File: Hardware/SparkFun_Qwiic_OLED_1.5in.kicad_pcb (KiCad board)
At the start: 2 copper layers, 34.3 x 48.3 mm, 59 parts, among them J1 Qwiic_RA, J2 Qwiic_RA, J3 Conn_01x06, U1 OLED_1.5in, U5 AP3012

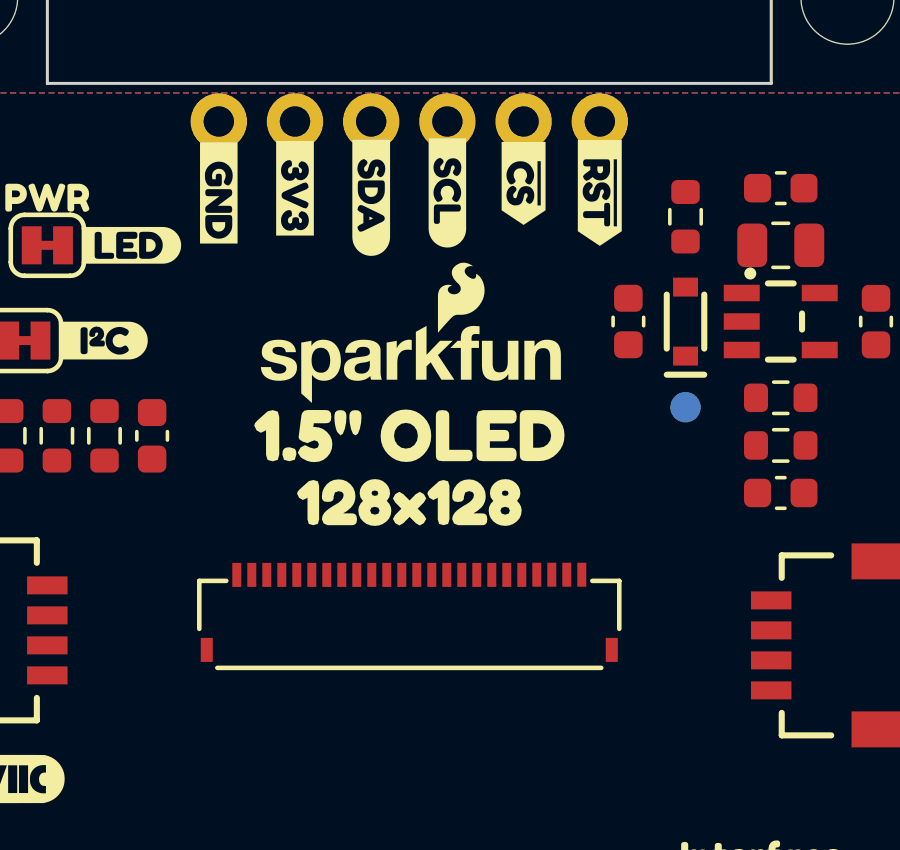
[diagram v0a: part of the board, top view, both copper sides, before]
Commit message: Removes connector from OLED symbol
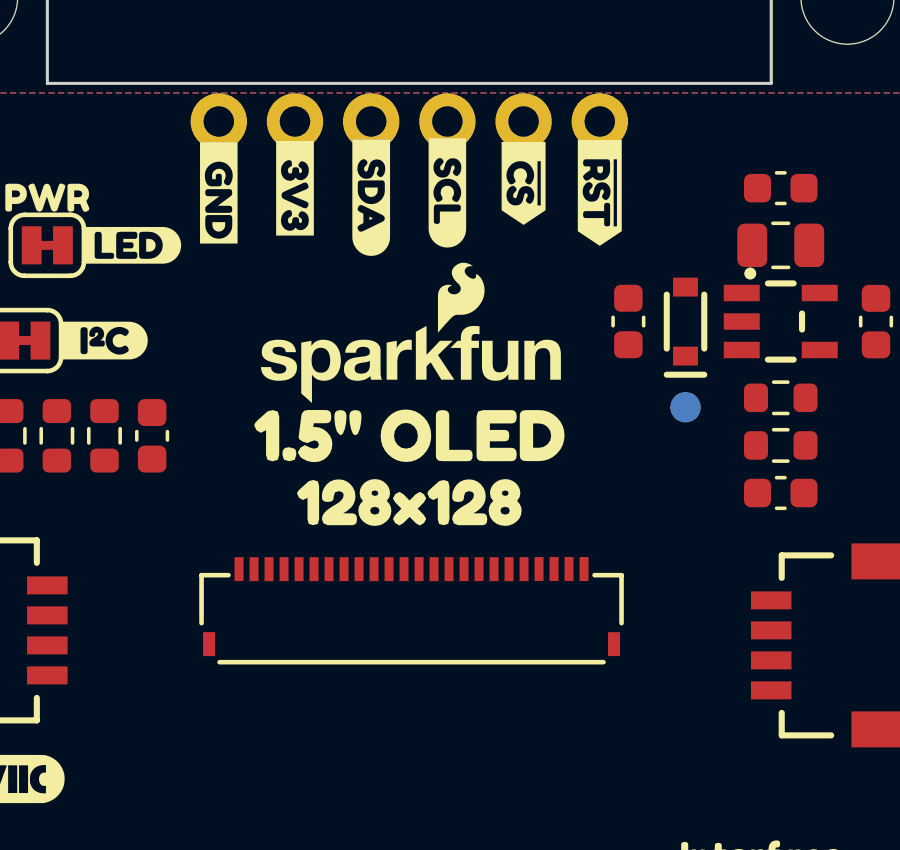
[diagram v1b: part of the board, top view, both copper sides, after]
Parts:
- removed R8: 10k, SparkFun-Resistor:R_0603_1608Metric
- removed U1: OLED_1.5in, SparkFun-Display:OLED_1.5in_128x128-Folded
- added J4: Conn_01x24_FPC, SparkFun-Connector:FPC_0.5mm-24, F.Cu at (140.5, 85.5)
- added U2: WEO128128ASAP3N00000, SparkFun-Display:OLED_1.5in_128x128-Folded, F.Cu at (140.4, 87.0)
- R6: value 634k -> 569k

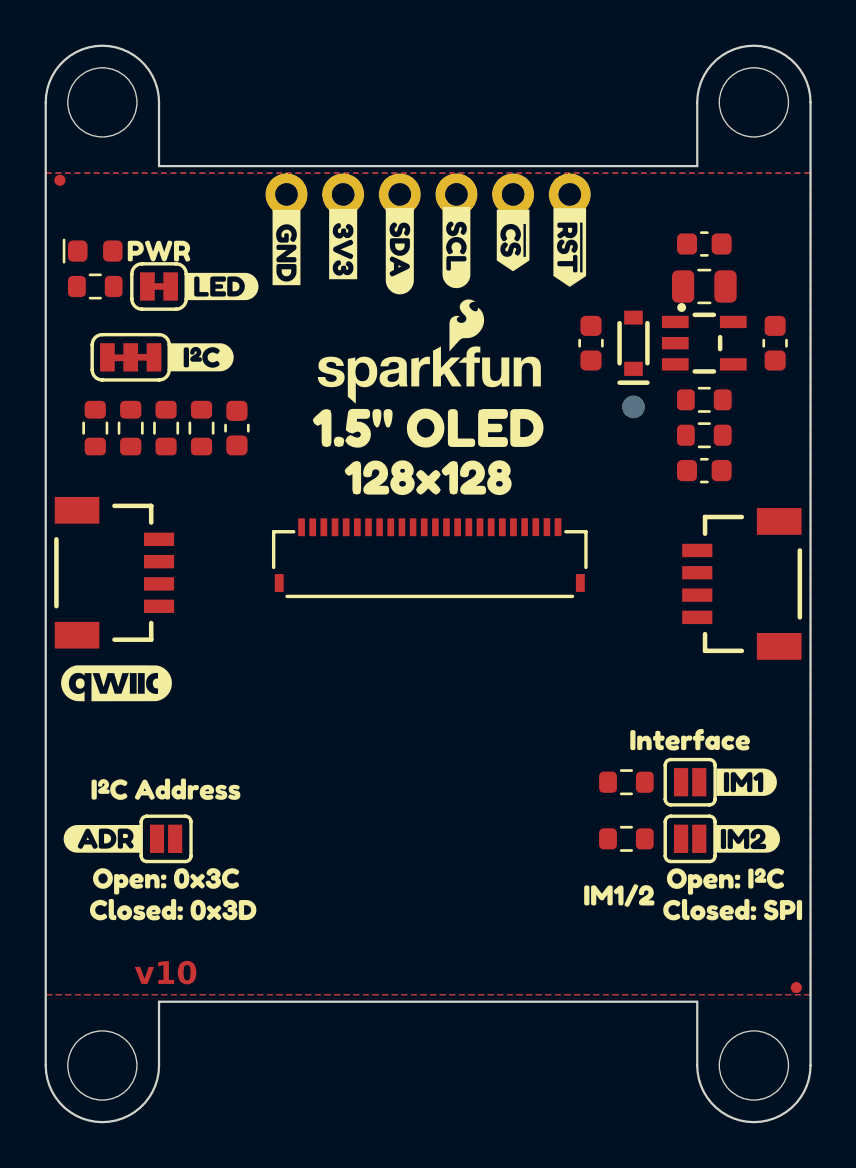
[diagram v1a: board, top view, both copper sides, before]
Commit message: Removes connector from OLED symbolbol and footprint
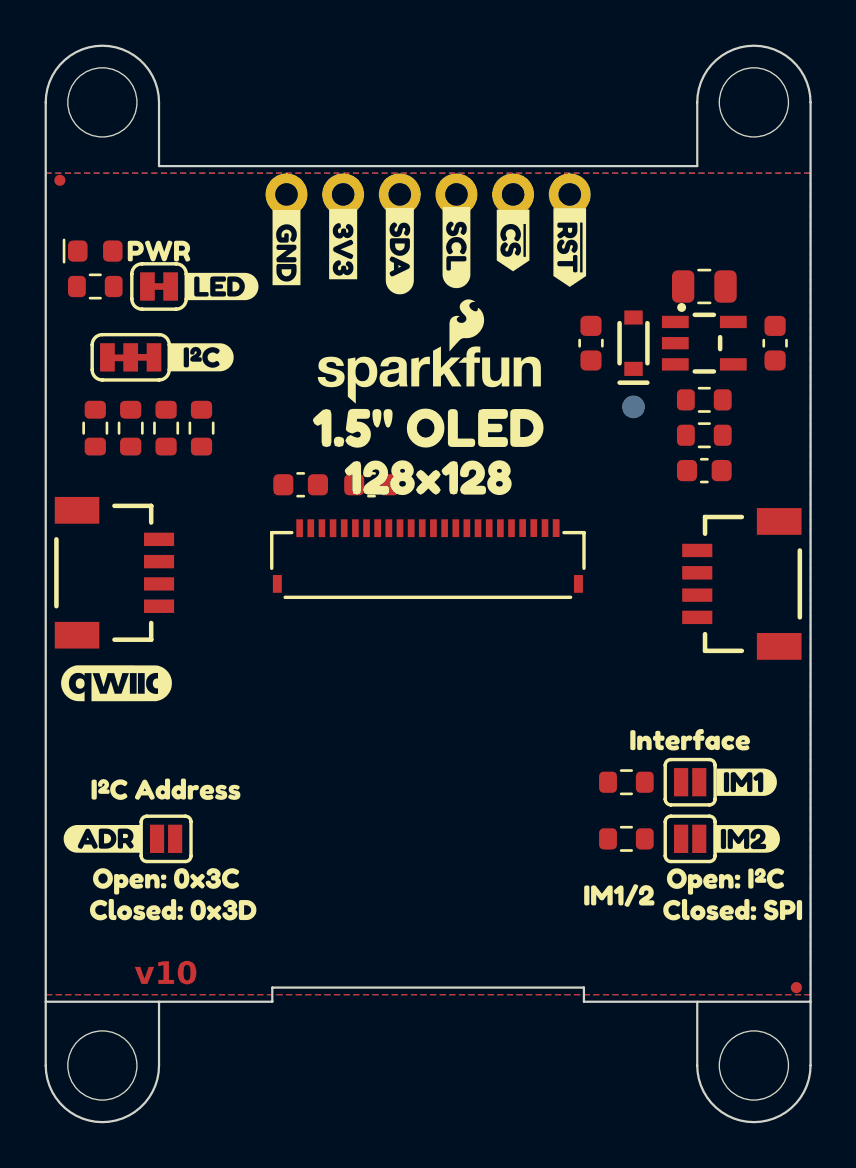
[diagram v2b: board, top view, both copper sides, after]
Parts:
- moved C4 18.4 mm to (137.9, 82.2), turned to 0 degrees
- moved C5 3.82 mm to (134.7, 82.2), turned to 180 degrees
- moved J4 0.10 mm to (140.4, 85.5)
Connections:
- J4 pad 13: unconnected-(J4-Pin_13-Pad13) -> GND
- J4 pad 14: unconnected-(J4-Pin_14-Pad14) -> GND
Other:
- outline, holes or cut-outs redrawn

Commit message: Aligns the power circuitry to the IC's specification
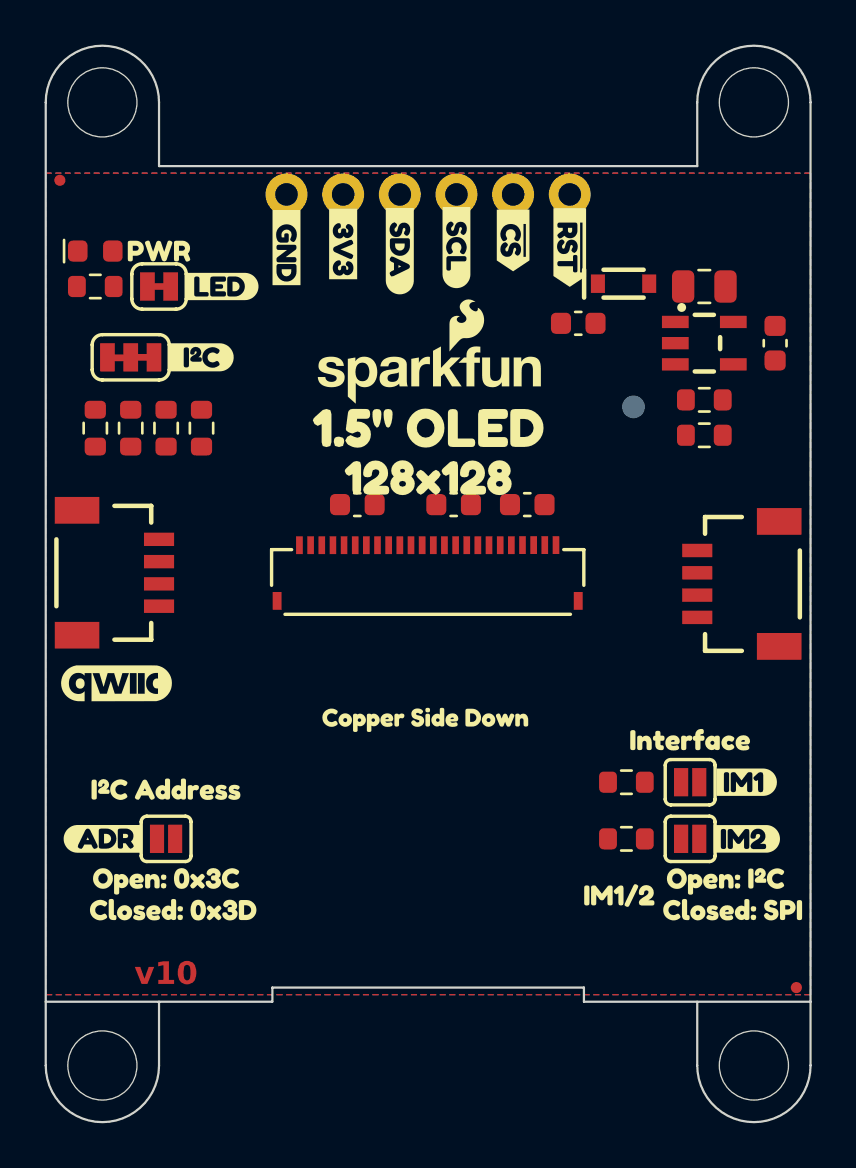
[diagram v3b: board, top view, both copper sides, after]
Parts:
- added kibuzzard-684C4DD6: G***, kibuzzard-684C4DD6, F.Cu at (140.3, 92.8)
- moved C3 15.6 mm to (137.2, 83.1)
- moved C5 10.2 mm to (144.9, 83.1)
- moved C4 3.79 mm to (141.6, 83.1), turned to 180 degrees
- moved D2 2.71 mm to (149.2, 73.2), turned to 0 degrees
- moved C2 1.06 mm to (147.1, 75.0), turned to 180 degrees
- moved J4 0.76 mm to (140.4, 86.3)
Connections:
- C3 pad 1: Net-(J4-Pin_3) -> Net-(J4-Pin_22)
- J4 pad 10: ~{CS} -> SCL/SCK
- J4 pad 11: ~{RST} -> GND
- J4 pad 12: Net-(J4-Pin_12) -> GND
- J4 pad 13: GND -> Net-(J4-Pin_13)
- J4 pad 14: GND -> ~{RST}
- J4 pad 15: SCL/SCK -> ~{CS}
- J4 pad 16: SDA/SDI -> Net-(J4-Pin_16)
- J4 pad 18: GND -> Net-(J4-Pin_18)
- J4 pad 19: GND -> Net-(J4-Pin_19)
- J4 pad 20: GND -> 3.3V
- J4 pad 21: GND -> 3.3V
- J4 pad 22: GND -> Net-(J4-Pin_22)
- J4 pad 3: Net-(J4-Pin_3) -> GND
- J4 pad 4: 3.3V -> GND
- J4 pad 5: 3.3V -> GND
- J4 pad 6: Net-(J4-Pin_6) -> GND
- J4 pad 7: Net-(J4-Pin_7) -> GND
- J4 pad 9: Net-(J4-Pin_9) -> SDA/SDI
- JP3 pad 1: Net-(J4-Pin_12) -> Net-(J4-Pin_13)
- JP6 pad 2: Net-(J4-Pin_6) -> Net-(J4-Pin_19)
- JP7 pad 1: Net-(J4-Pin_7) -> Net-(J4-Pin_18)
- R10 pad 2: Net-(J4-Pin_6) -> Net-(J4-Pin_19)
- R11 pad 1: Net-(J4-Pin_7) -> Net-(J4-Pin_18)
- R6 pad 2: Net-(J4-Pin_9) -> Net-(J4-Pin_16)
- R7 pad 2: Net-(J4-Pin_12) -> Net-(J4-Pin_13)

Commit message: Routes the power circuitry
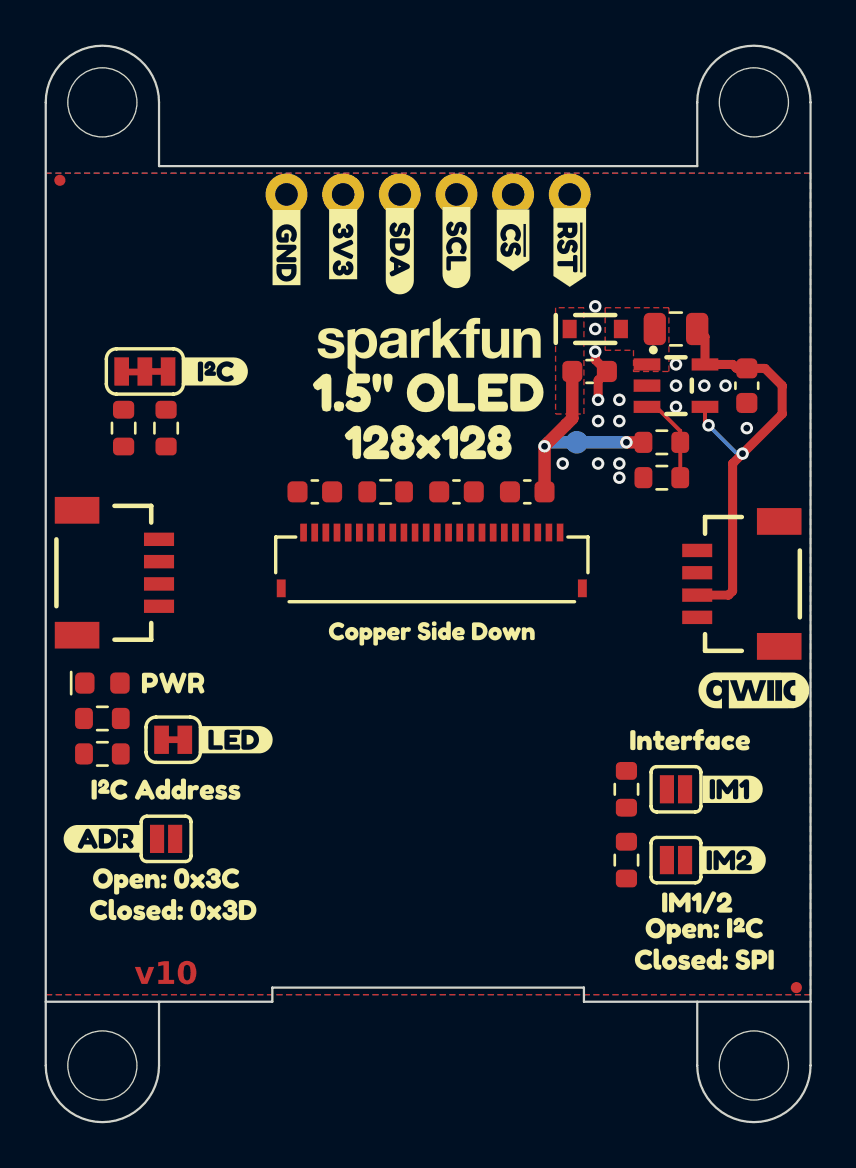
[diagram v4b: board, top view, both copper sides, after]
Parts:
- removed the G*** at (140.4, 77.2)
- added G***: LOGO, SparkFun-Aesthetic:SparkFun_Logo_NoFlame_10mm, F.Cu at (140.4, 75.9)
- moved G*** 28.6 mm to (155.0, 91.4)
- moved JP1 20.3 mm to (129.0, 93.7)
- moved kibuzzard-680FC883 20.3 mm to (131.8, 93.7)
- moved kibuzzard-65A8A8B4 19.4 mm to (129.0, 91.1)
- moved R3 19.4 mm to (125.8, 92.7)
- moved D1 19.4 mm to (125.8, 91.1)
- moved R7 14.9 mm to (125.8, 94.3), turned to 0 degrees
- moved R6 8.74 mm to (138.5, 82.5), turned to 0 degrees
- moved kibuzzard-684C4DD6 3.88 mm to (140.6, 88.9)
- moved kibuzzard-680FC9DC 3.51 mm to (152.5, 101.0)
- moved TP1 3.00 mm to (147.1, 80.3)
- moved R12 2.69 mm to (150.9, 80.3)
- moved R9 2.69 mm to (150.9, 81.9)
- moved kibuzzard-680FCA02 2.56 mm to (152.8, 103.5)
- moved kibuzzard-680FCAD6 2.42 mm to (152.8, 102.2)
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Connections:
- net Net-(D2-A) renamed 12V_OUT
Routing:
- net 3.3V: track 0.00 -> 20.8 mm, vias 0 -> 2
- net 12V: track 0.00 -> 10.1 mm, vias 0 -> 2
- net Net-(U5-FB): track 0.00 -> 4.03 mm
- net GND: track 0.00 -> 2.54 mm, vias 0 -> 17
- added copper zone on F.Cu, net 12V
- added copper zone on F.Cu, net 12V_OUT

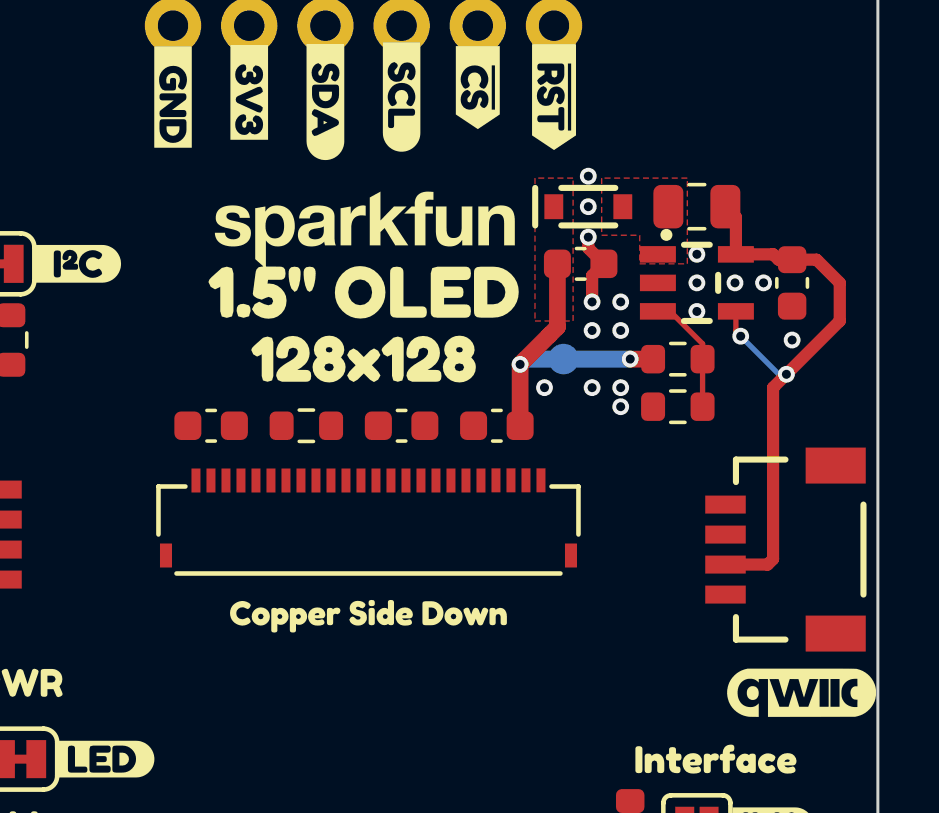
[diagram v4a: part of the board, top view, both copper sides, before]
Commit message: Adds another pour for 3.3V at the power circuitry
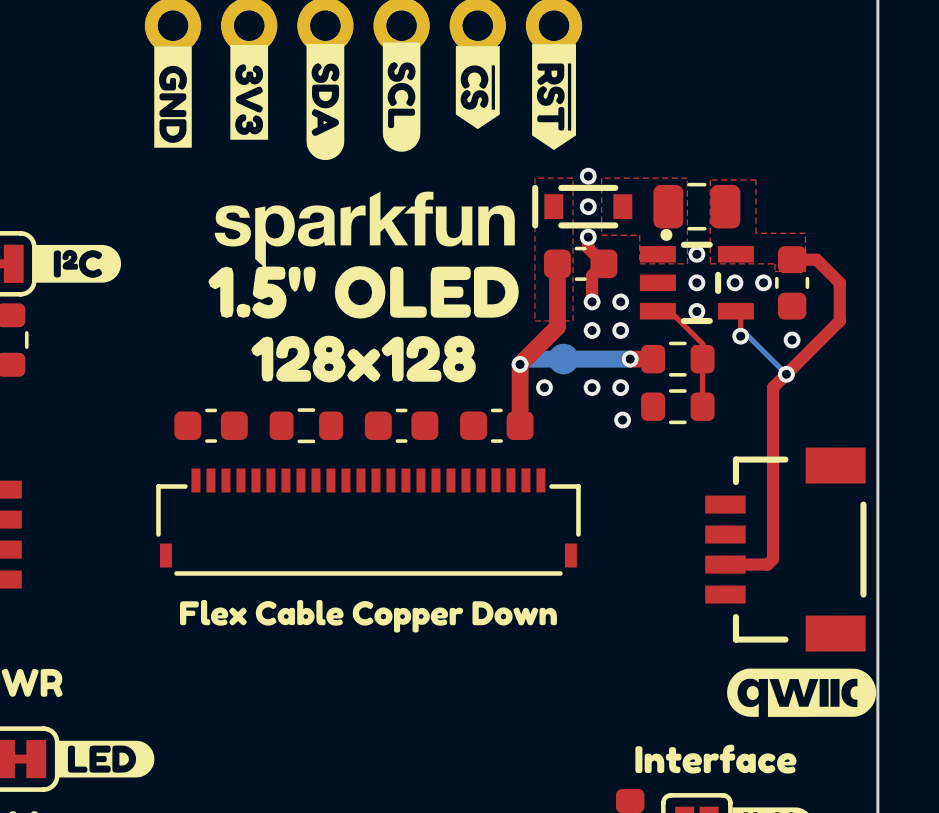
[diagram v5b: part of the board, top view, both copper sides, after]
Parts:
- removed kibuzzard-684C4DD6: G***, kibuzzard-684C4DD6
- added kibuzzard-684C656A: G***, kibuzzard-684C656A, F.Cu at (140.6, 88.9)
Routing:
- net 3.3V: track 20.8 -> 17.1 mm
- added copper zone on F.Cu, net 3.3V
